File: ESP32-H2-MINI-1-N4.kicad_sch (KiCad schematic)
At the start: 13 parts, among them U1 ESP32-H2-MINI-1-N4

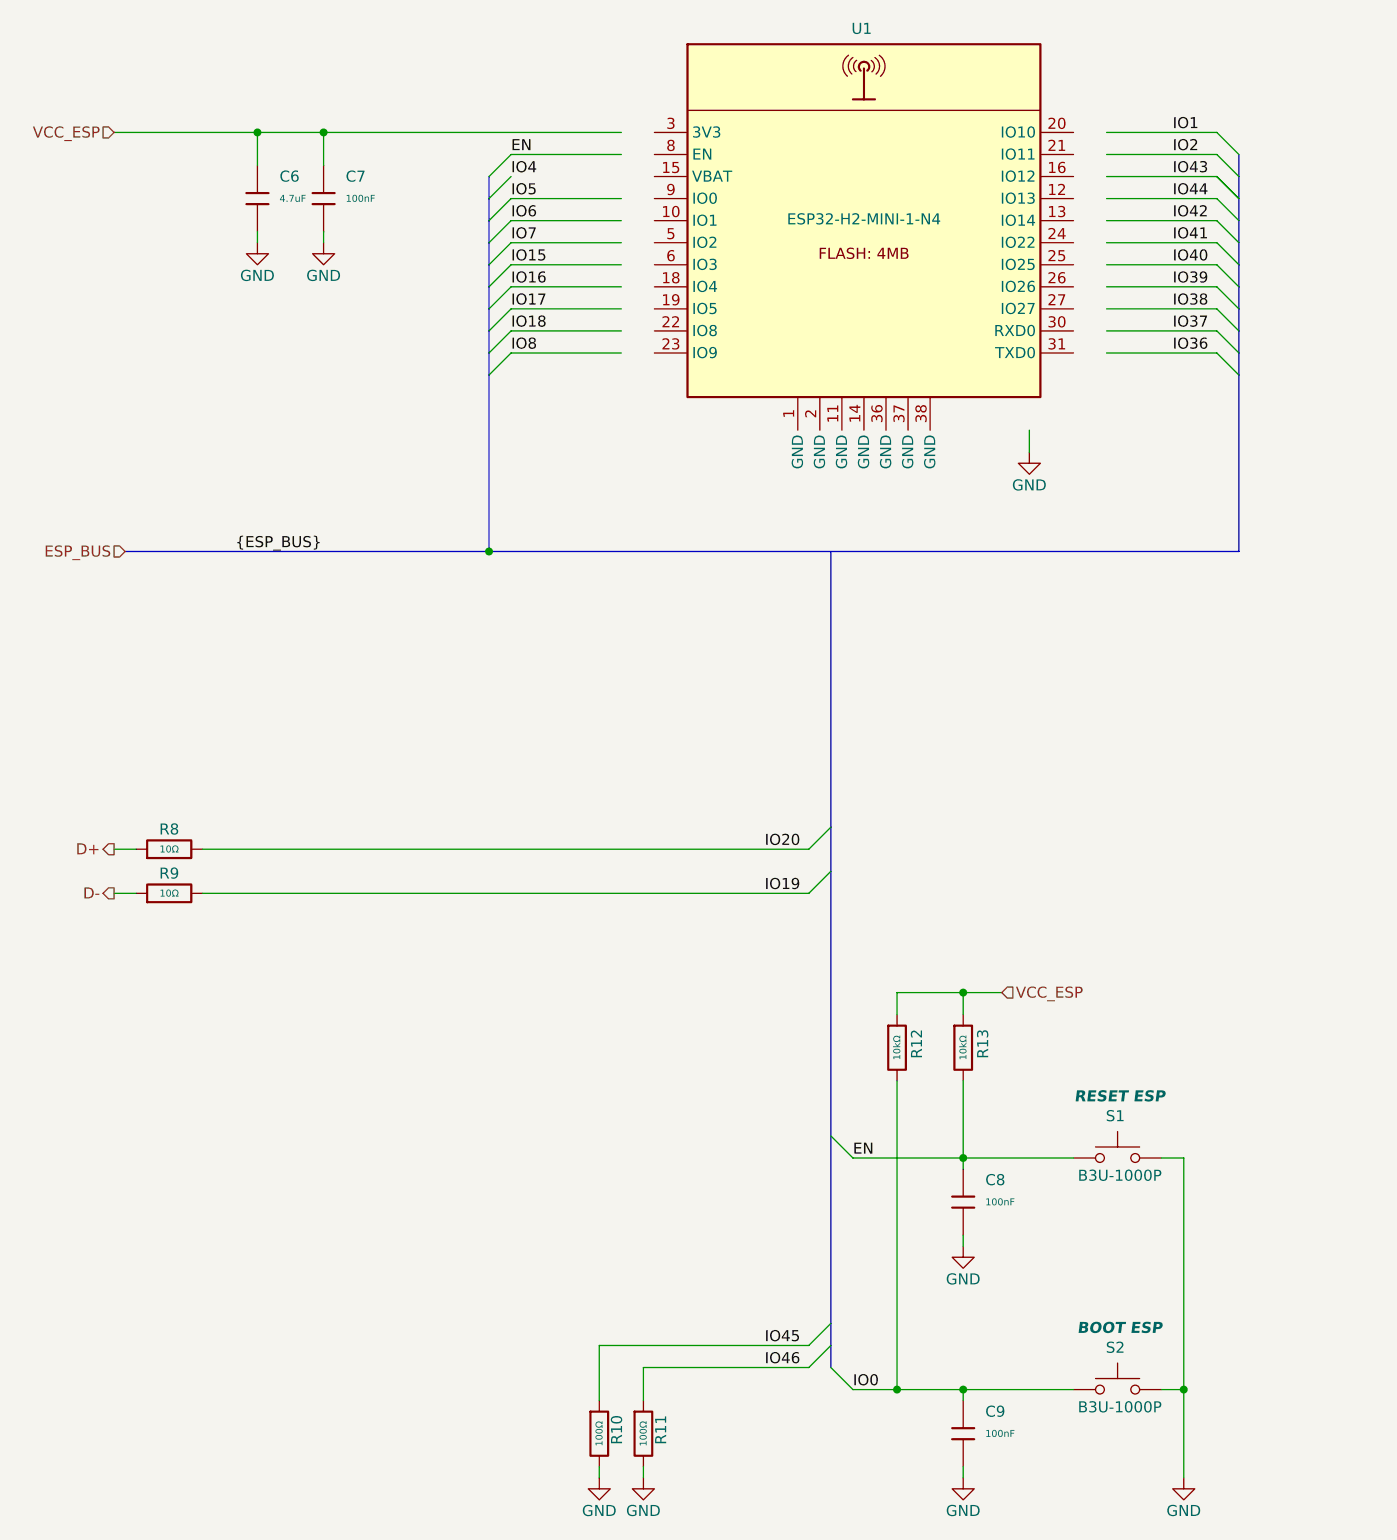
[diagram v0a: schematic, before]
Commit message: H2-Board: C6/S3-Werkbank-Blätter raus, H2-Subsheet auf neuen Block-Stand (ESP32-H2-MINI-1-N4)
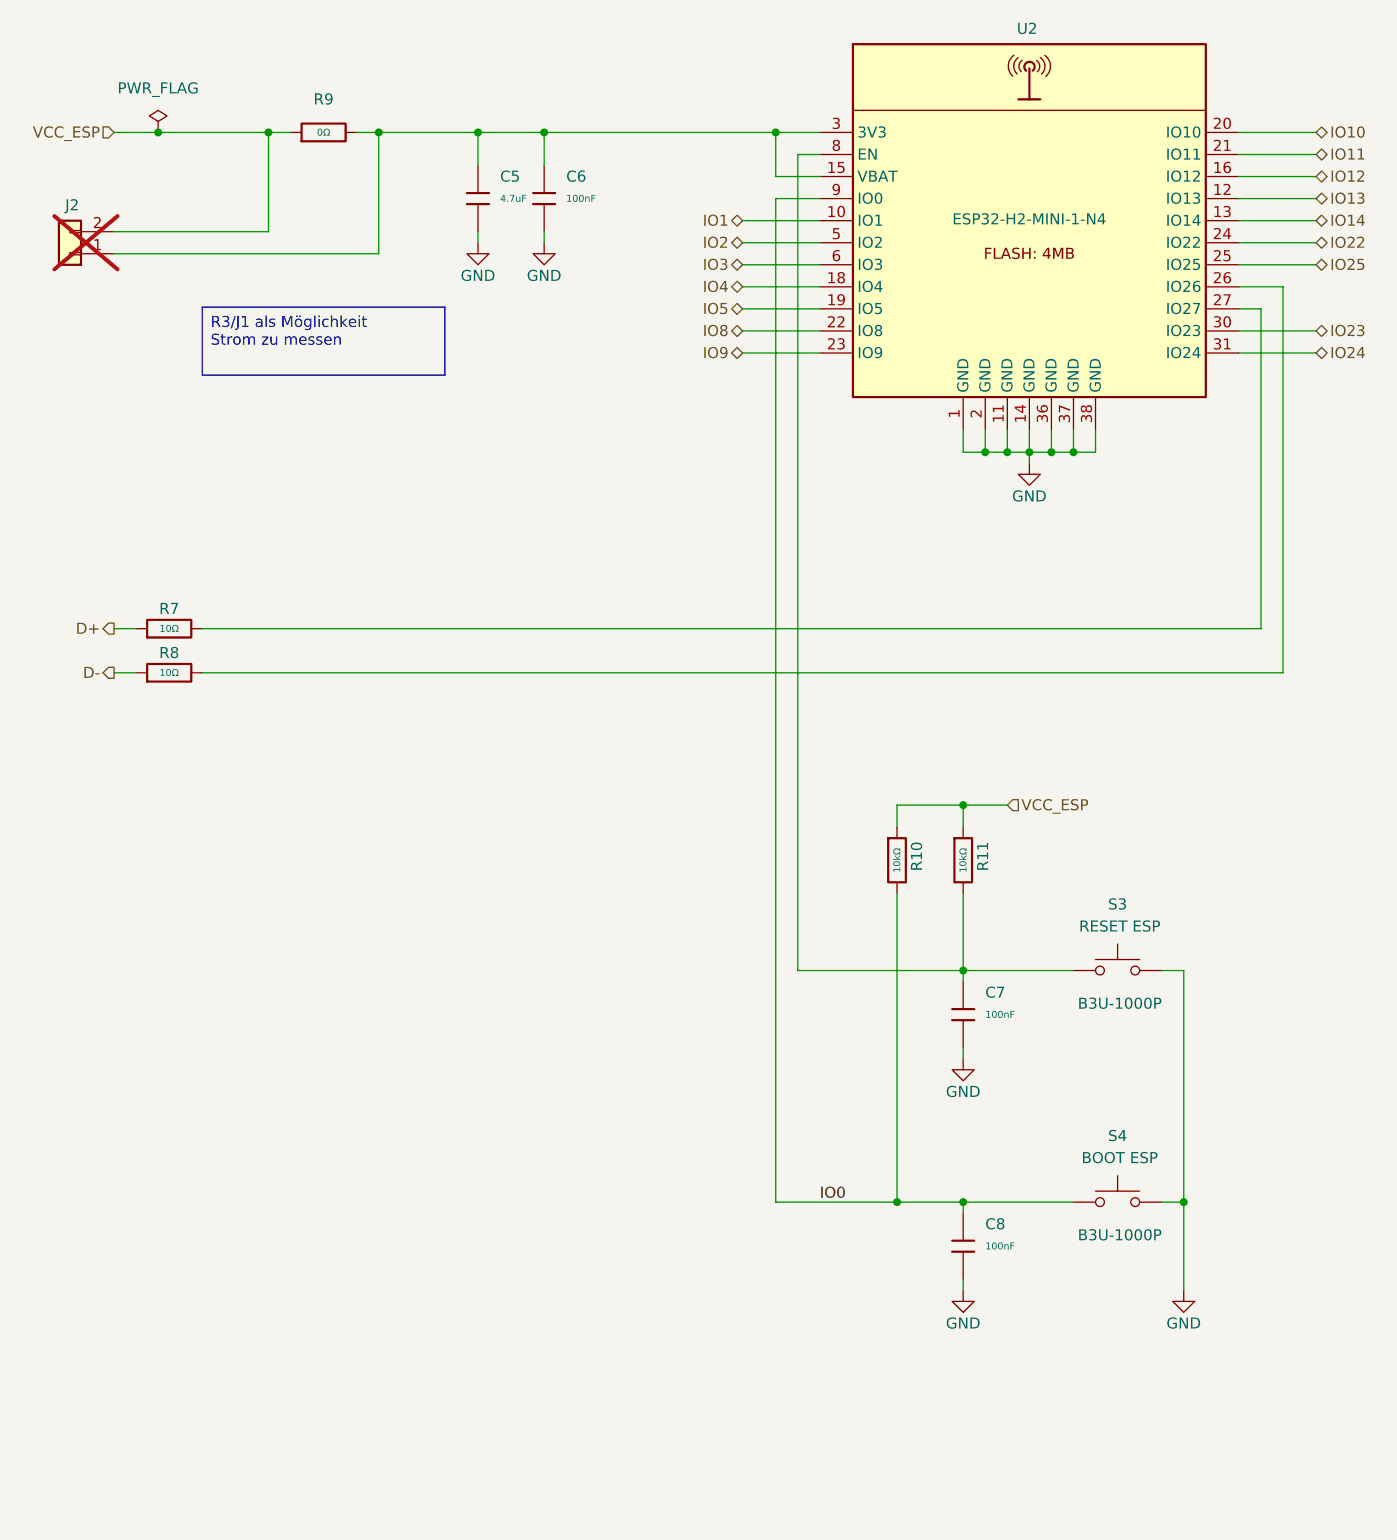
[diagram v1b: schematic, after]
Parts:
- removed R10, R11: 100Ω, PCM_JLCPCB:R_0603, symbol PCM_JLCPCB-Resistors:0603,100Ω
- removed S1, S2: B3U-1000P, SMD:B3U-1000P, symbol switch_wie:SW_Push_mini_SMD_B3U-1000P
- added J2: Conn_01x02, Connector_PinHeader_2.54mm:PinHeader_1x02_P2.54mm_Vertical, symbol Connector_Generic:Conn_01x02
- added R9: 0Ω, PCM_JLCPCB:R_0603, symbol PCM_JLCPCB-Resistors:0603,0Ω
- added S3, S4: B3U-1000P, jlcpcb:KEY-SMD_B3U-1000PM, symbol DL1DTU_B3U-1000P:SW_Push_mini_SMD_B3U-1000P
- U2: renamed from U1; footprint jlcpcb:WIFIM-SMD_61P-L16.6-W13.2-P0.80-ESP32-C6-MINI-1-N4 -> Espressif:ESP32-H2-MINI-1
- renumbered C6 to C5, C7 to C6, C8 to C7, C9 to C8, R12 to R10, R13 to R11, R8 to R7, R9 to R8
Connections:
- net EN is gone; now on an unnamed net: C7.1, R11.2
- net IO19 is gone; now on an unnamed net: R8.2
- net IO20 is gone; now on an unnamed net: R7.2
- net GND: now also U2.11 (GND), U2.14 (GND), U2.2 (GND), U2.36 (GND), U2.37 (GND), U2.38 (GND), S3.2, S4.2
- net IO0: now also U2.9 (IO0), S4.1
- net IO1: now also U2.10 (IO1)
- net IO2: now also U2.5 (IO2)
- net IO4: now also U2.18 (IO4)
- net IO5: now also U2.19 (IO5)
- net IO8: now also U2.22 (IO8)
- net VCC_ESP: now also J2.2 (Pin_2), R9.1; no longer C5.1, C6.1
- net IO13: now reaches U2.12 (IO13)
- net IO14: now reaches U2.13 (IO14)
- net at U2.15 (VBAT): now also C5.1, C6.1, U2.3 (3V3), J2.1 (Pin_1), R9.2
- net IO12: now reaches U2.16 (IO12)
- net IO10: now reaches U2.20 (IO10)
- net IO11: now reaches U2.21 (IO11)
- net IO9: now reaches U2.23 (IO9)
- net IO22: now reaches U2.24 (IO22)
- net IO25: now reaches U2.25 (IO25)
- net IO23: now reaches U2.30 (IO23)
- net IO24: now reaches U2.31 (IO24)
- net IO3: now reaches U2.6 (IO3)
- net at U2.8 (EN): now also S3.1
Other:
- moved on the sheet: C5, C6, C7, C8, R10, R11, R7, R8, U2

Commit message: Migration PCM_JLCPCB- -> JLCPCB_ (Symbole aus Submodule)
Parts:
- C5: symbol PCM_JLCPCB-Capacitors:0603,4.7uF -> JLCPCB_Capacitors:0603,4.7uF; Stock 4246728 -> 5643370
- C6, C7, C8: symbol PCM_JLCPCB-Capacitors:0603,100nF -> JLCPCB_Capacitors:0603,100nF; Stock 70324515 -> 37493696
- R10, R11: symbol PCM_JLCPCB-Resistors:0603,10kΩ -> JLCPCB_Resistors:0603,10kΩ; Price 0.004USD -> 0.005USD; Stock 51181774 -> 22319909
- R7, R8: symbol PCM_JLCPCB-Resistors:0603,10Ω -> JLCPCB_Resistors:0603,10Ω; Price 0.004USD -> 0.005USD; Stock 5764851 -> 2613887
- R9: symbol PCM_JLCPCB-Resistors:0603,0Ω -> JLCPCB_Resistors:0603,0Ω; Price 0.004USD -> 0.005USD; Stock 7706573 -> 13902554
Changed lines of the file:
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@@
 	)
 	(symbol
-		(lib_id "PCM_JLCPCB-Resistors:0603,0Ω")
+		(lib_id "JLCPCB_Resistors:0603,0Ω")
 		(at 58.42 30.48 90)
 		(unit 1)
@@
 			)
 		)
-		(property "Description" "100mW Thick Film Resistors 75V ±1% 0Ω 0603 Chip Resistor - Surface Mount ROHS"
+		(property "Description" "-55°C~+155°C 0Ω 100mW 75V Thick Film Resistor ±1% 0603 Chip Resistor - Surface Mount ROHS"
 			(at 58.42 30.48 0)
 			(hide yes)
@@
 			)
 		)
-		(property "Stock" "7706573"
+		(property "Stock" "13902554"
 			(at 58.42 30.48 0)
 			(hide yes)
@@
 			)
 		)
-		(property "Price" "0.004USD"
+		(property "Price" "0.005USD"
 			(at 58.42 30.48 0)
 			(hide yes)
@@
 	)
 	(symbol
-		(lib_id "PCM_JLCPCB-Capacitors:0603,100nF")
+		(lib_id "JLCPCB_Capacitors:0603,100nF")
 		(at 132.08 158.75 0)
 		(unit 1)
@@
 			)
 		)
-		(property "Description" "50V 100nF X7R ±10% 0603 Multilayer Ceramic Capacitors MLCC - SMD/SMT ROHS"
+		(property "Description" "100nF 50V X7R ±10% 0603 Multilayer Ceramic Capacitors MLCC - SMD/SMT ROHS"
 			(at 132.08 158.75 0)
 			(hide yes)
@@
 			)
 		)
-		(property "Stock" "70324515"
+		(property "Stock" "37493696"
 			(at 132.08 158.75 0)
 			(hide yes)
@@
 	)
 	(symbol
-		(lib_id "PCM_JLCPCB-Resistors:0603,10kΩ")
+		(lib_id "JLCPCB_Resistors:0603,10kΩ")
 		(at 132.08 114.3 0)
 		(unit 1)
@@
 			)
 		)
-		(property "Description" "100mW Thick Film Resistors 75V ±100ppm/°C ±1% 10kΩ 0603 Chip Resistor - Surface Mount ROHS"
+		(property "Description" "-55°C~+155°C 100mW 10kΩ 75V Thick Film Resistor ±1% ±100ppm/°C 0603 Chip Resistor - Surface Mount ROHS"
 			(at 132.08 114.3 0)
 			(hide yes)
@@
 			)
 		)
-		(property "Stock" "51181774"
+		(property "Stock" "22319909"
 			(at 132.08 114.3 0)
 			(hide yes)
@@
 			)
 		)
-		(property "Price" "0.004USD"
+		(property "Price" "0.005USD"
 			(at 132.08 114.3 0)
 			(hide yes)
@@
 	)
 	(symbol
-		(lib_id "PCM_JLCPCB-Capacitors:0603,4.7uF")
+		(lib_id "JLCPCB_Capacitors:0603,4.7uF")
 		(at 76.2 38.1 0)
 		(unit 1)
@@
 			)
 		)
-		(property "Stock" "4246728"
+		(property "Stock" "5643370"
 			(at 76.2 38.1 0)
 			(hide yes)
@@
 	)
 	(symbol
-		(lib_id "PCM_JLCPCB-Capacitors:0603,100nF")
+		(lib_id "JLCPCB_Capacitors:0603,100nF")
 		(at 132.08 132.08 0)
 		(unit 1)
@@
 			)
 		)
-		(property "Description" "50V 100nF X7R ±10% 0603 Multilayer Ceramic Capacitors MLCC - SMD/SMT ROHS"
+		(property "Description" "100nF 50V X7R ±10% 0603 Multilayer Ceramic Capacitors MLCC - SMD/SMT ROHS"
 			(at 132.08 132.08 0)
 			(hide yes)
@@
 			)
 		)
-		(property "Stock" "70324515"
+		(property "Stock" "37493696"
 			(at 132.08 132.08 0)
 			(hide yes)
@@
 	)
 	(symbol
-		(lib_id "PCM_JLCPCB-Resistors:0603,10kΩ")
+		(lib_id "JLCPCB_Resistors:0603,10kΩ")
 		(at 124.46 114.3 0)
 		(unit 1)
@@
 			)
 		)
-		(property "Description" "100mW Thick Film Resistors 75V ±100ppm/°C ±1% 10kΩ 0603 Chip Resistor - Surface Mount ROHS"
+		(property "Description" "-55°C~+155°C 100mW 10kΩ 75V Thick Film Resistor ±1% ±100ppm/°C 0603 Chip Resistor - Surface Mount ROHS"
 			(at 124.46 114.3 0)
 			(hide yes)
@@
 			)
 		)
-		(property "Stock" "51181774"
+		(property "Stock" "22319909"
 			(at 124.46 114.3 0)
 			(hide yes)
@@
 			)
 		)
-		(property "Price" "0.004USD"
+		(property "Price" "0.005USD"
 			(at 124.46 114.3 0)
 			(hide yes)
@@
 	)
 	(symbol
-		(lib_id "PCM_JLCPCB-Resistors:0603,10Ω")
+		(lib_id "JLCPCB_Resistors:0603,10Ω")
 		(at 40.64 92.71 90)
 		(unit 1)
@@
 			)
 		)
-		(property "Description" "100mW Thick Film Resistors 75V ±1% ±400ppm/°C 10Ω 0603 Chip Resistor - Surface Mount ROHS"
+		(property "Description" "-55°C~+155°C 100mW 10Ω 75V Thick Film Resistor ±1% ±400ppm/°C 0603 Chip Resistor - Surface Mount ROHS"
 			(at 40.64 92.71 0)
 			(hide yes)
@@
 			)
 		)
-		(property "Stock" "5764851"
+		(property "Stock" "2613887"
 			(at 40.64 92.71 0)
 			(hide yes)
@@
 			)
 		)
-		(property "Price" "0.004USD"
+		(property "Price" "0.005USD"
 			(at 40.64 92.71 0)
 			(hide yes)
@@
 	)
 	(symbol
-		(lib_id "PCM_JLCPCB-Resistors:0603,10Ω")
+		(lib_id "JLCPCB_Resistors:0603,10Ω")
 		(at 40.64 87.63 90)
 		(unit 1)
@@
 			)
 		)
-		(property "Description" "100mW Thick Film Resistors 75V ±1% ±400ppm/°C 10Ω 0603 Chip Resistor - Surface Mount ROHS"
+		(property "Description" "-55°C~+155°C 100mW 10Ω 75V Thick Film Resistor ±1% ±400ppm/°C 0603 Chip Resistor - Surface Mount ROHS"
 			(at 40.64 87.63 0)
 			(hide yes)
@@
 			)
 		)
-		(property "Stock" "5764851"
+		(property "Stock" "2613887"
 			(at 40.64 87.63 0)
 			(hide yes)
@@
 			)
 		)
-		(property "Price" "0.004USD"
+		(property "Price" "0.005USD"
 			(at 40.64 87.63 0)
 			(hide yes)
@@
 	)
 	(symbol
-		(lib_id "PCM_JLCPCB-Capacitors:0603,100nF")
+		(lib_id "JLCPCB_Capacitors:0603,100nF")
 		(at 83.82 38.1 0)
 		(unit 1)
@@
 			)
 		)
-		(property "Description" "50V 100nF X7R ±10% 0603 Multilayer Ceramic Capacitors MLCC - SMD/SMT ROHS"
+		(property "Description" "100nF 50V X7R ±10% 0603 Multilayer Ceramic Capacitors MLCC - SMD/SMT ROHS"
 			(at 83.82 38.1 0)
 			(hide yes)
@@
 			)
 		)
-		(property "Stock" "70324515"
+		(property "Stock" "37493696"
 			(at 83.82 38.1 0)
 			(hide yes)
